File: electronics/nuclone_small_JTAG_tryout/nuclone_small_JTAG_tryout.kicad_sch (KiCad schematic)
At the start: 54 parts, among them J3 nuclone_small_left, J4 nuclone_small_right, J5 FTDI_PINS_1X06, J6 DevBoardUartInput

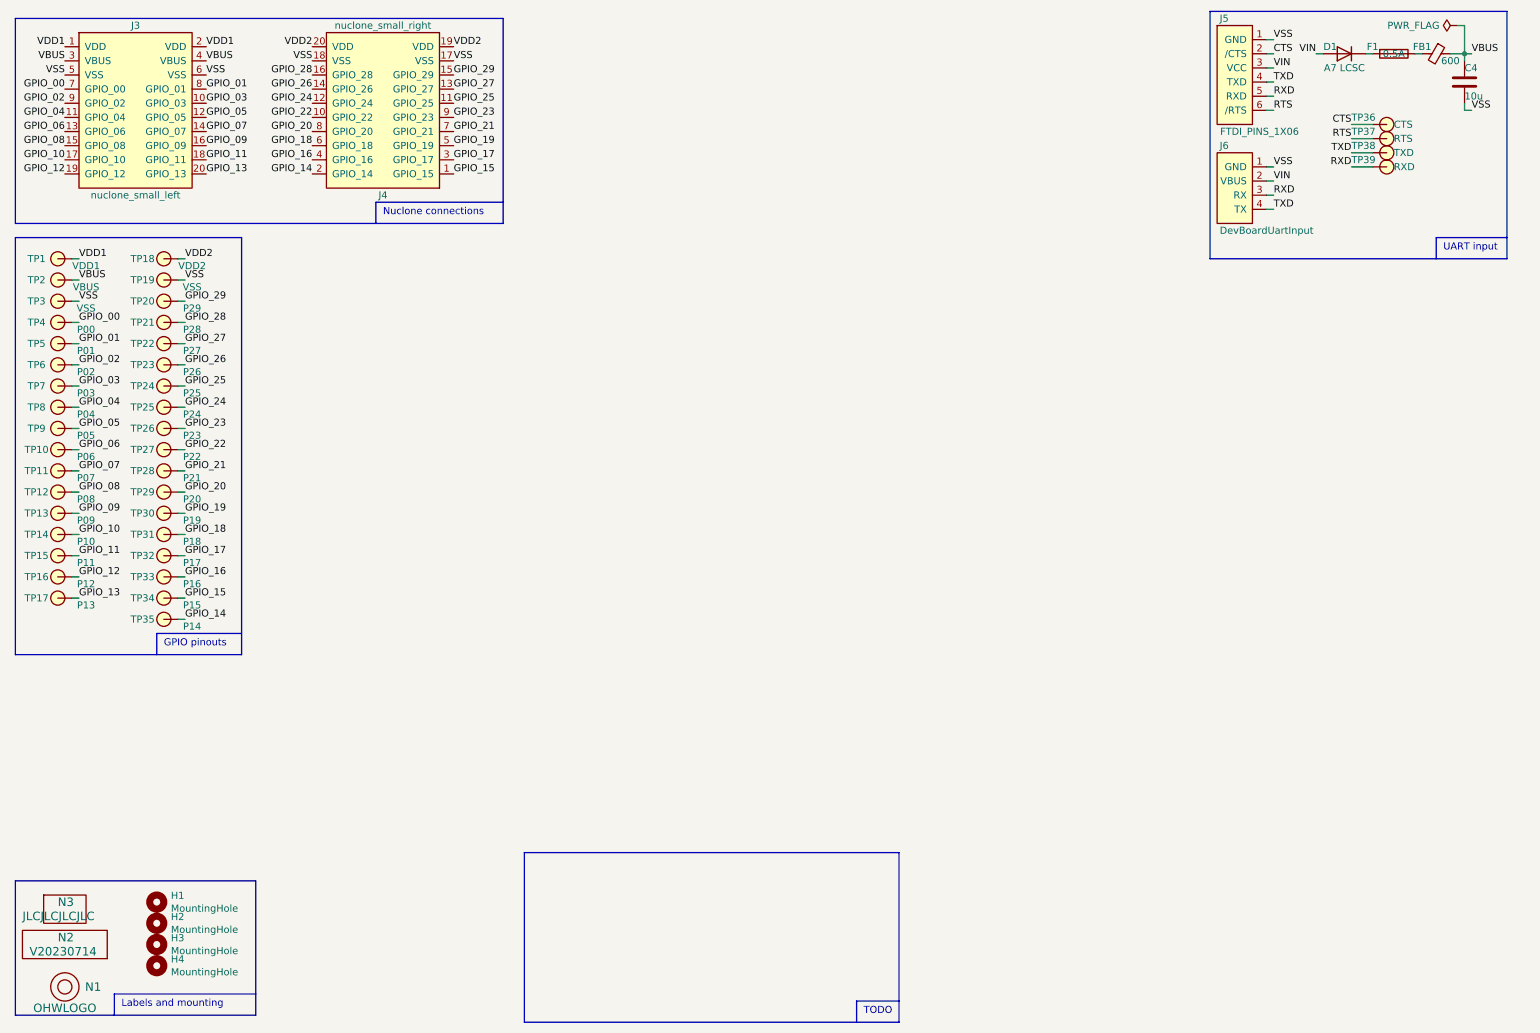
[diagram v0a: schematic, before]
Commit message: WIP schematic entry: added reset control/detection and power control/detection
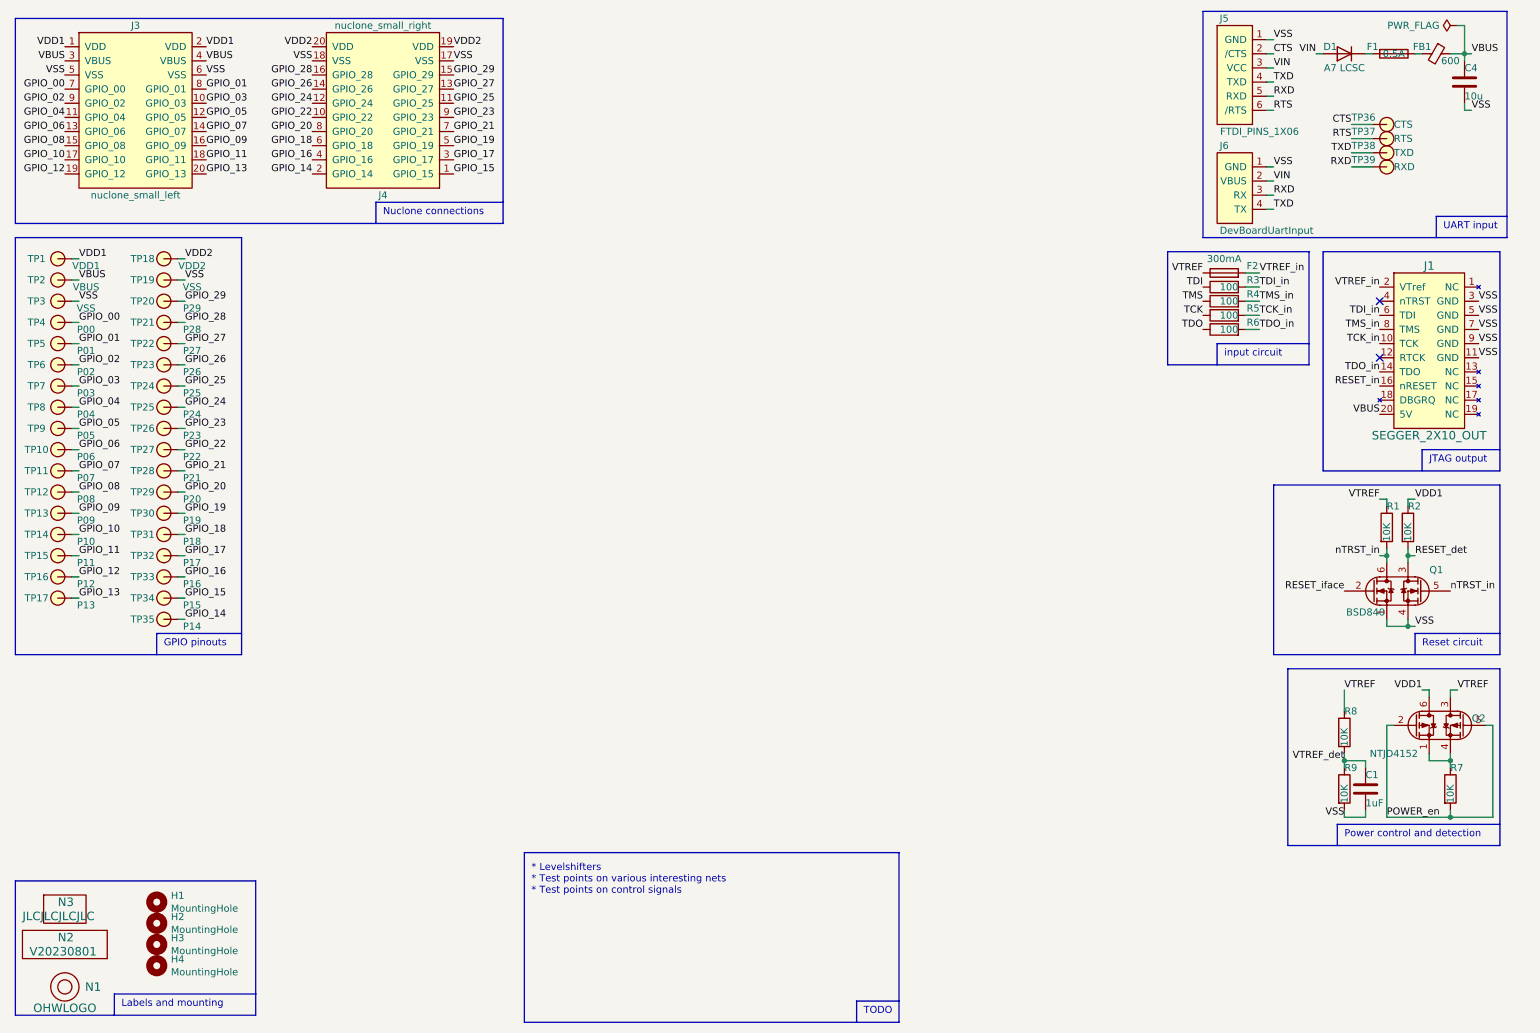
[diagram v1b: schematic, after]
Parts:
- added C1: 1uF, SquantorRcl:C_0603, symbol Device:C
- added F2: 300mA, SquantorRcl:F_0603_hand, symbol Device:Fuse
- added J1: SEGGER_2X10_OUT, SquantorConnectors:Header-0254-2X10-H010, symbol SquantorConnectorsNamed:SEGGER_2X10_OUT
- added Q1: BSD840, SquantorIC:SOT363-NXP-hand, symbol SquantorDevice:Q_NMOS_DUAL
- added Q2: NTJD4152, SquantorIC:SOT363-NXP-hand, symbol SquantorDevice:Q_PMOS_DUAL
- added R1, R2, R7, R8, R9: 10K, SquantorRcl:R_0603_hand, symbol Device:R
- added R3, R4, R5, R6: 100, SquantorRcl:R_0603_hand, symbol Device:R
- N2: value V20230714 -> V20230801
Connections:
- net VBUS: now also J1.20 (5V)
- net VDD1: now also Q2.6 (D1), R2.1
- net VSS: now also C1.2, J1.11 (GND), J1.3 (GND), J1.5 (GND), J1.7 (GND), J1.9 (GND), Q1.1 (S1), Q1.4 (S2), R9.2
- new net: Q2.1 (S1), Q2.4 (S2), R7.1
- new net POWER_en: Q2.2 (G1), Q2.5 (G2), R7.2
- new net RESET_det: Q1.3 (D2), R2.2
- new net RESET_iface: Q1.2 (G1)
- new net RESET_in: J1.16 (nRESET)
- new net TCK: R5.1
- new net TCK_in: J1.10 (TCK), R5.2
- new net TDI: R3.1
- new net TDI_in: J1.6 (TDI), R3.2
- new net TDO: R6.1
- new net TDO_in: J1.14 (TDO), R6.2
- new net TMS: R4.1
- new net TMS_in: J1.8 (TMS), R4.2
- new net VTREF: F2.1, Q2.3 (D2), R1.1, R8.1
- new net VTREF_det: C1.1, R8.2, R9.1
- new net VTREF_in: F2.2, J1.2 (VTref)
- new net nTRST_in: Q1.5 (G2), Q1.6 (D1), R1.2
- no-connect marks 0 -> 2
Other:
- note added: "* Levelshifters * Test points on various interesting nets * Test points on control signals"
- note added: "JTAG output"
- note added: "Power control and detection"
- note added: "Reset circuit"
- note added: "input circuit"
